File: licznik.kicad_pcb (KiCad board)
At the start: 2 copper layers, 71.1 x 44.8 mm, 24 parts, among them J1 Display, J2 Micro_SD_Card_Det, J3 Serial CS1, J4 Serial CS2, SW1 Wheel, SW2 Crank, SW3 Backlight, SW4 Right, SW5 Select, SW6 Left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

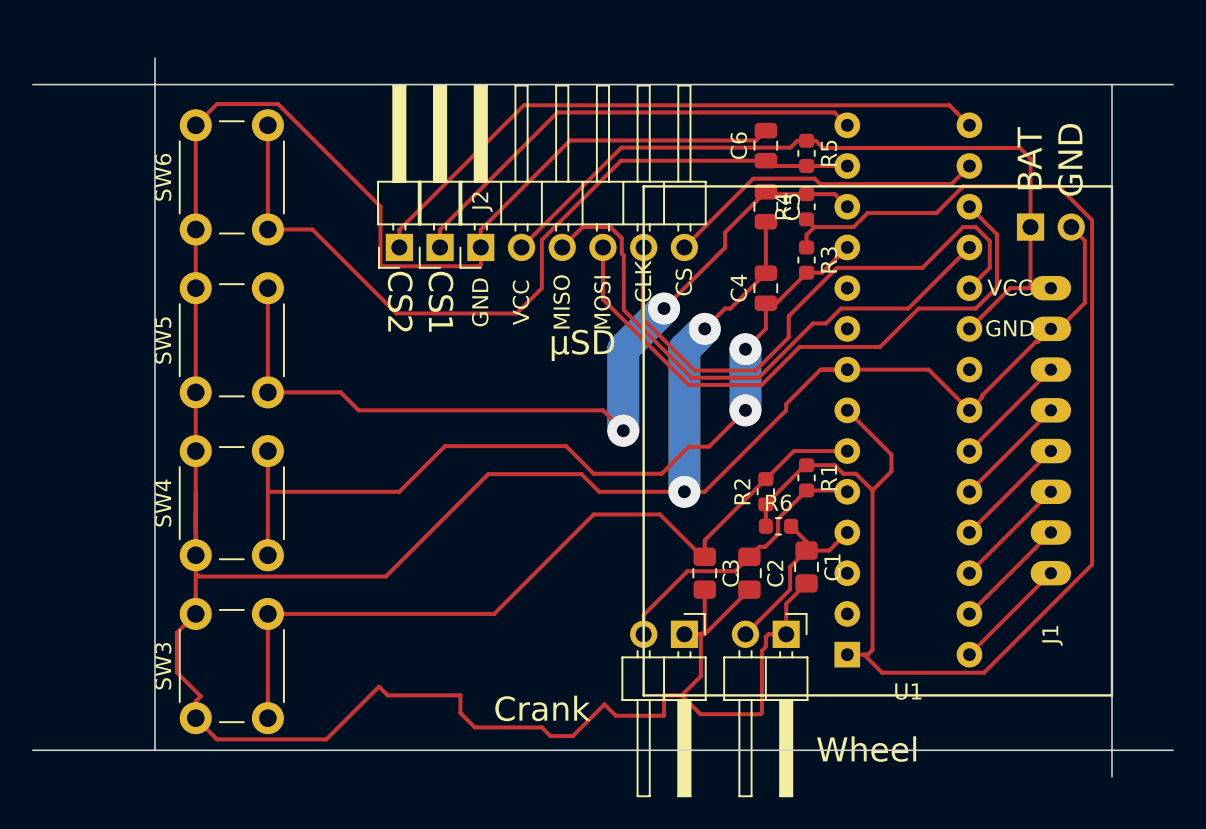
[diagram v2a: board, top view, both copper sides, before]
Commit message: Added elements for accelerometers, updated Nokia screen, shrunk the board
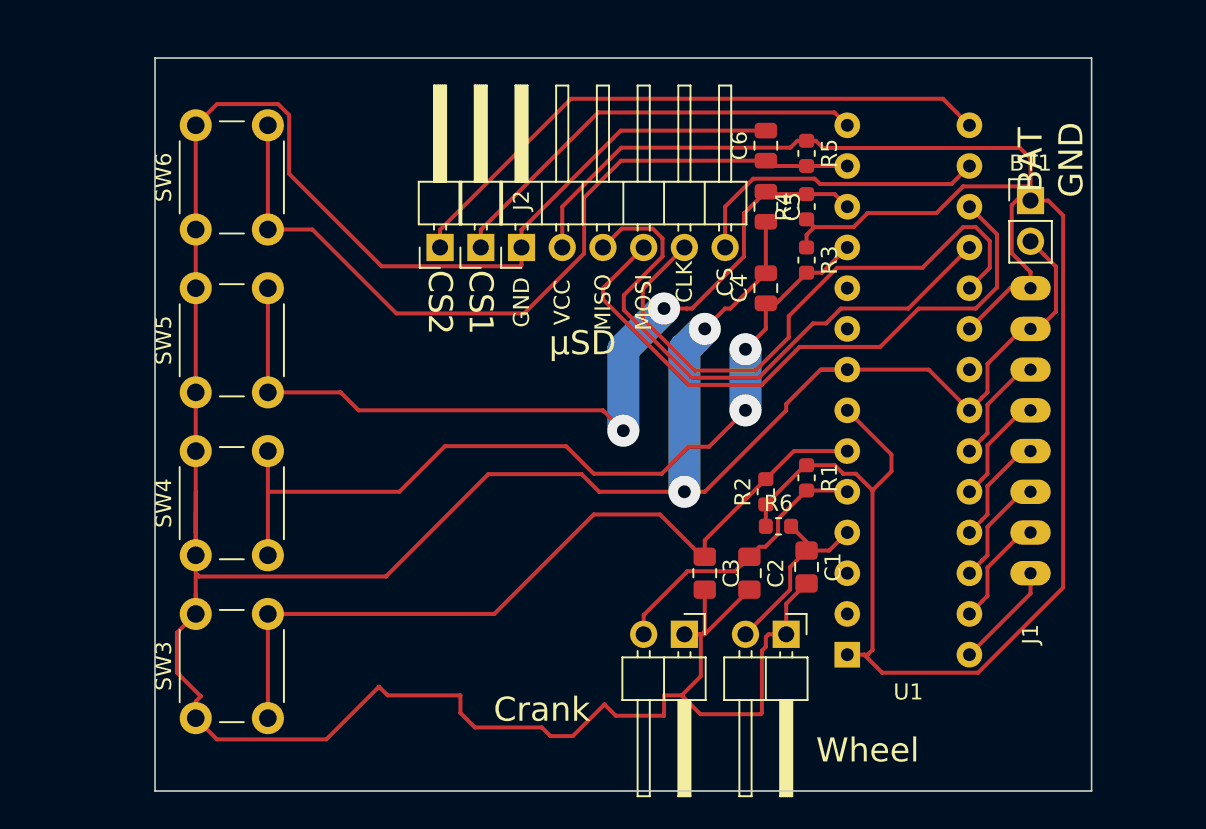
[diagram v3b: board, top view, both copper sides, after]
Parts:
- BT1: moved to F.Cu
- moved J1 5.39 mm to (87.6, 178.2)
- moved J3 2.54 mm to (53.3, 166.8)
- moved J2 2.54 mm to (55.9, 166.8)
- moved J4 2.54 mm to (50.8, 166.8)
- moved BT1 1.66 mm to (87.6, 163.8), turned to 0 degrees
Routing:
- net +BATT: track 139.3 -> 134.1 mm
- net Net-(J3-Pad1): track 29.9 -> 27.3 mm
- net Net-(J4-Pad1): track 40.4 -> 38.2 mm
- net GND: track 249.1 -> 248.0 mm
- net Net-(J2-Pad2): track 20.2 -> 19.1 mm
- net Net-(J2-Pad5): track 35.8 -> 36.8 mm
- net Net-(J2-Pad3): track 38.3 -> 39.3 mm
- net Net-(C5-Pad1): track 53.7 -> 54.7 mm
- net Net-(J2-Pad7): track 35.7 -> 36.6 mm
- net Net-(J1-Pad8): track 7.18 -> 6.66 mm
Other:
- board size 71.1 x 44.8 mm -> 58.4 x 45.7 mm

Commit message: Moved buttons closer to the middle
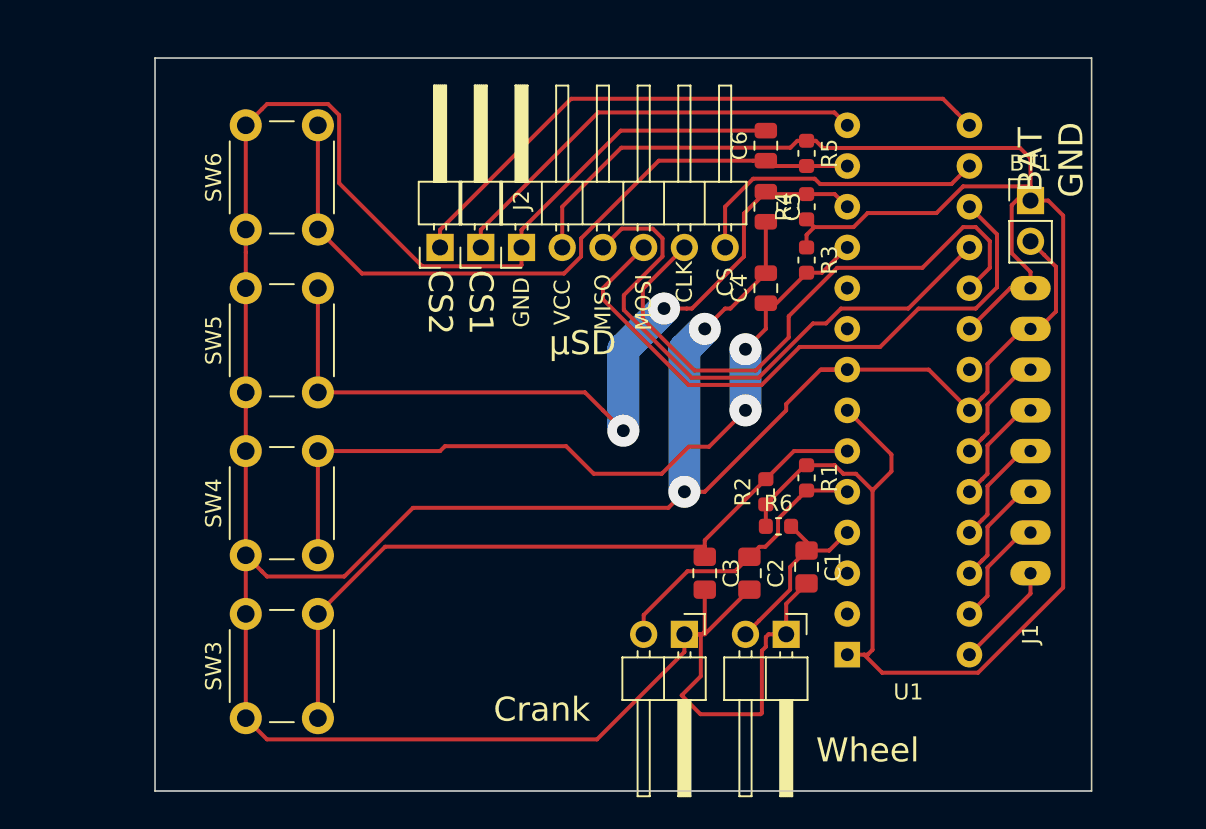
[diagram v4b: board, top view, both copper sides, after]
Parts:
- moved SW3 3.12 mm to (38.7, 196.1)
- moved SW4 3.12 mm to (38.7, 186.0)
- moved SW5 3.12 mm to (38.7, 175.8)
- moved SW6 3.12 mm to (38.7, 165.6)
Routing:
- net GND: track 248.0 -> 228.7 mm
- net Net-(C6-Pad1): track 50.9 -> 44.4 mm
- net Net-(C3-Pad1): track 50.2 -> 45.1 mm
- net Net-(C4-Pad1): track 53.3 -> 49.2 mm
- net Net-(C5-Pad1): track 54.7 -> 51.6 mm

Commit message: Spaced around components for easy soldering
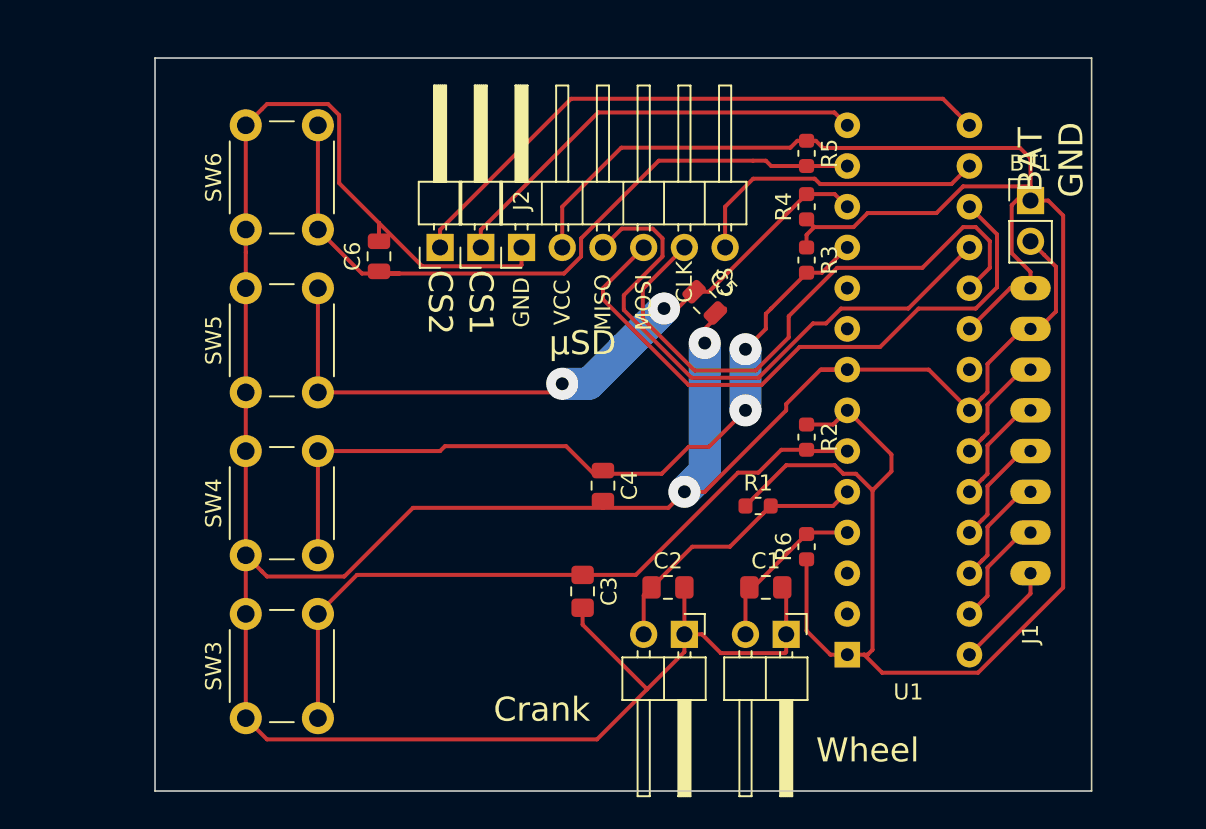
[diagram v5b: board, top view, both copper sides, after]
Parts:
- moved C6 25.1 mm to (47.0, 167.3)
- moved C4 16.0 mm to (61.0, 181.6), turned to 270 degrees
- moved C3 7.70 mm to (59.7, 188.2)
- moved C5 7.08 mm to (67.3, 170.2), turned to 315 degrees
- moved C2 5.16 mm to (65.0, 188.0), turned to 0 degrees
- moved R2 4.25 mm to (73.7, 178.6), turned to 270 degrees
- moved R1 3.49 mm to (70.6, 182.9), turned to 0 degrees
- moved C1 2.84 mm to (71.1, 188.0), turned to 0 degrees
- moved R6 2.16 mm to (73.7, 185.4), turned to 90 degrees
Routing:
- net GND: track 228.7 -> 195.6 mm
- net +BATT: track 134.1 -> 144.5 mm
- net Net-(C5-Pad1): track 51.6 -> 45.0 mm
- net Net-(C3-Pad1): track 45.1 -> 43.8 mm
- net Net-(C6-Pad1): track 44.4 -> 45.7 mm
- net Net-(C1-Pad1): track 11.7 -> 10.6 mm

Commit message: Added screen mounting holes
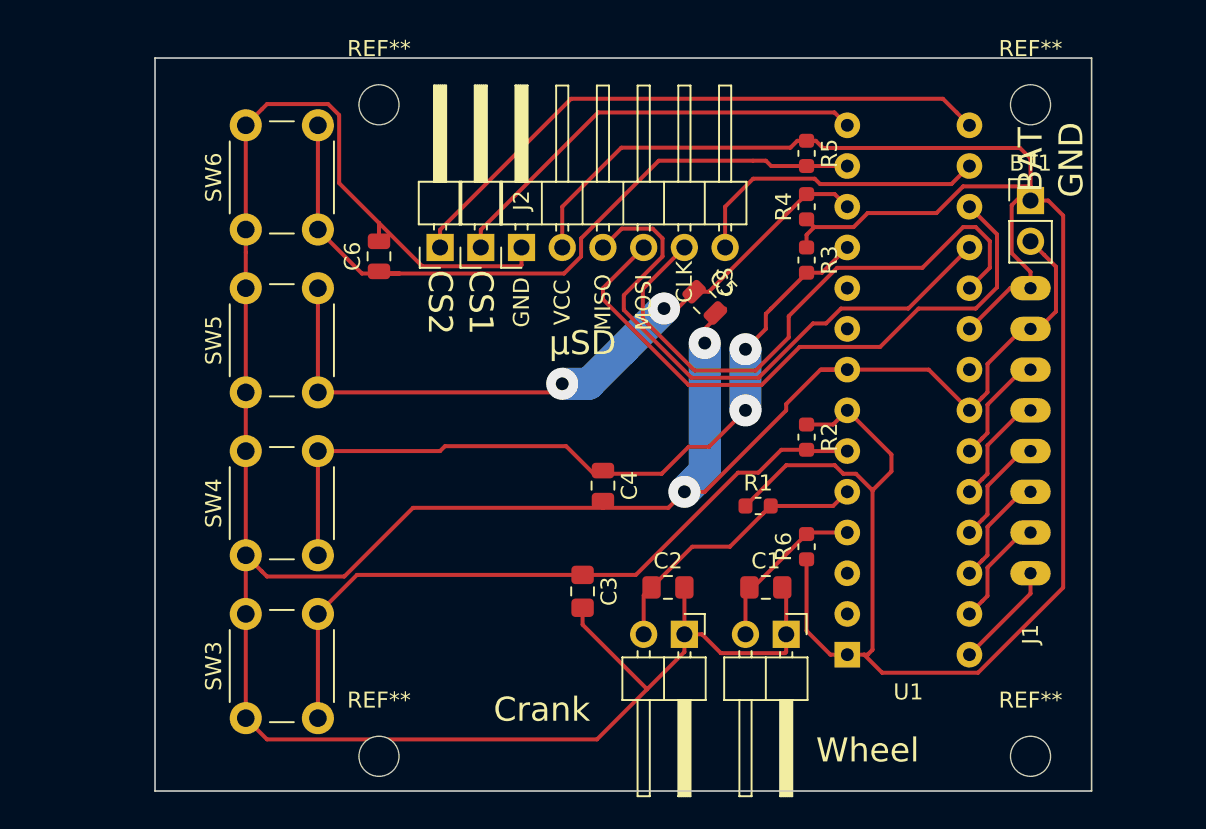
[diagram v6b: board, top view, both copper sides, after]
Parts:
- added REF**: MountingHole_2.5mm, MountingHole:MountingHole_2.5mm, F.Cu at (47.0, 157.9)
- added REF**: MountingHole_2.5mm, MountingHole:MountingHole_2.5mm, F.Cu at (87.6, 157.9)
- added REF**: MountingHole_2.5mm, MountingHole:MountingHole_2.5mm, F.Cu at (87.6, 198.5)
- added REF**: MountingHole_2.5mm, MountingHole:MountingHole_2.5mm, F.Cu at (47.0, 198.5)
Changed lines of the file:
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@@
     (tracks 264)
     (zones 0)
-    (modules 24)
+    (modules 28)
     (nets 26)
   )
@@
     (solder_mask_min_width 0.25)
     (aux_axis_origin 128.778 126.746)
-    (visible_elements FFFFFF7F)
+    (visible_elements FFFFFFFF)
     (pcbplotparams
       (layerselection 0x00030_80000001)
@@
     (uvia_drill 0.1)
   )
+  (module MountingHole:MountingHole_2.5mm (layer F.Cu)
+    (at 46.99 157.855)
+    (descr "Mounting Hole 2.5mm, no annular")
+    (tags "mounting hole 2.5mm no annular")
+    (attr virtual)
+    (fp_text reference REF** (at 0 -3.5) (layer F.SilkS)
+      (effects (font (size 1 1) (thickness 0.15)))
+    )
+    (fp_text value MountingHole_2.5mm (at 0 3.5) (layer F.Fab)
+      (effects (font (size 1 1) (thickness 0.15)))
+    )
+    (fp_text user %R (at 0.3 0) (layer F.Fab)
+      (effects (font (size 1 1) (thickness 0.15)))
+    )
+    (fp_circle (center 0 0) (end 2.5 0) (layer Cmts.User) (width 0.15))
+    (fp_circle (center 0 0) (end 2.75 0) (layer F.CrtYd) (width 0.05))
+    (pad 1 np_thru_hole circle (at 0 0) (size 2.5 2.5) (drill 2.5) (layers *.Cu *.Mask))
+  )
+  (module MountingHole:MountingHole_2.5mm (layer F.Cu)
+    (at 87.63 157.855)
+    (descr "Mounting Hole 2.5mm, no annular")
+    (tags "mounting hole 2.5mm no annular")
+    (attr virtual)
+    (fp_text reference REF** (at 0 -3.5) (layer F.SilkS)
+      (effects (font (size 1 1) (thickness 0.15)))
+    )
+    (fp_text value MountingHole_2.5mm (at 0 3.5) (layer F.Fab)
+      (effects (font (size 1 1) (thickness 0.15)))
+    )
+    (fp_text user %R (at 0.3 0) (layer F.Fab)
+      (effects (font (size 1 1) (thickness 0.15)))
+    )
+    (fp_circle (center 0 0) (end 2.5 0) (layer Cmts.User) (width 0.15))
+    (fp_circle (center 0 0) (end 2.75 0) (layer F.CrtYd) (width 0.05))
+    (pad 1 np_thru_hole circle (at 0 0) (size 2.5 2.5) (drill 2.5) (layers *.Cu *.Mask))
+  )
+  (module MountingHole:MountingHole_2.5mm (layer F.Cu)
+    (at 87.63 198.495)
+    (descr "Mounting Hole 2.5mm, no annular")
+    (tags "mounting hole 2.5mm no annular")
+    (attr virtual)
+    (fp_text reference REF** (at 0 -3.5) (layer F.SilkS)
+      (effects (font (size 1 1) (thickness 0.15)))
+    )
+    (fp_text value MountingHole_2.5mm (at 0 3.5) (layer F.Fab)
+      (effects (font (size 1 1) (thickness 0.15)))
+    )
+    (fp_text user %R (at 0.3 0) (layer F.Fab)
+      (effects (font (size 1 1) (thickness 0.15)))
+    )
+    (fp_circle (center 0 0) (end 2.5 0) (layer Cmts.User) (width 0.15))
+    (fp_circle (center 0 0) (end 2.75 0) (layer F.CrtYd) (width 0.05))
+    (pad 1 np_thru_hole circle (at 0 0) (size 2.5 2.5) (drill 2.5) (layers *.Cu *.Mask))
+  )
+  (module MountingHole:MountingHole_2.5mm (layer F.Cu)
+    (at 46.99 198.495)
+    (descr "Mounting Hole 2.5mm, no annular")
+    (tags "mounting hole 2.5mm no annular")
+    (attr virtual)
+    (fp_text reference REF** (at 0 -3.5) (layer F.SilkS)
+      (effects (font (size 1 1) (thickness 0.15)))
+    )
+    (fp_text value MountingHole_2.5mm (at 0 3.5) (layer F.Fab)
+      (effects (font (size 1 1) (thickness 0.15)))
+    )
+    (fp_circle (center 0 0) (end 2.75 0) (layer F.CrtYd) (width 0.05))
+    (fp_circle (center 0 0) (end 2.5 0) (layer Cmts.User) (width 0.15))
+    (fp_text user %R (at 0.3 0) (layer F.Fab)
+      (effects (font (size 1 1) (thickness 0.15)))
+    )
+    (pad 1 np_thru_hole circle (at 0 0) (size 2.5 2.5) (drill 2.5) (layers *.Cu *.Mask))
+  )
   (module "Licznik:Nokia screen" (layer F.Cu)

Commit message: Added logo
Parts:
- added logo: G***, Licznik:logo_half, F.Cu at (53.3, 191.8)

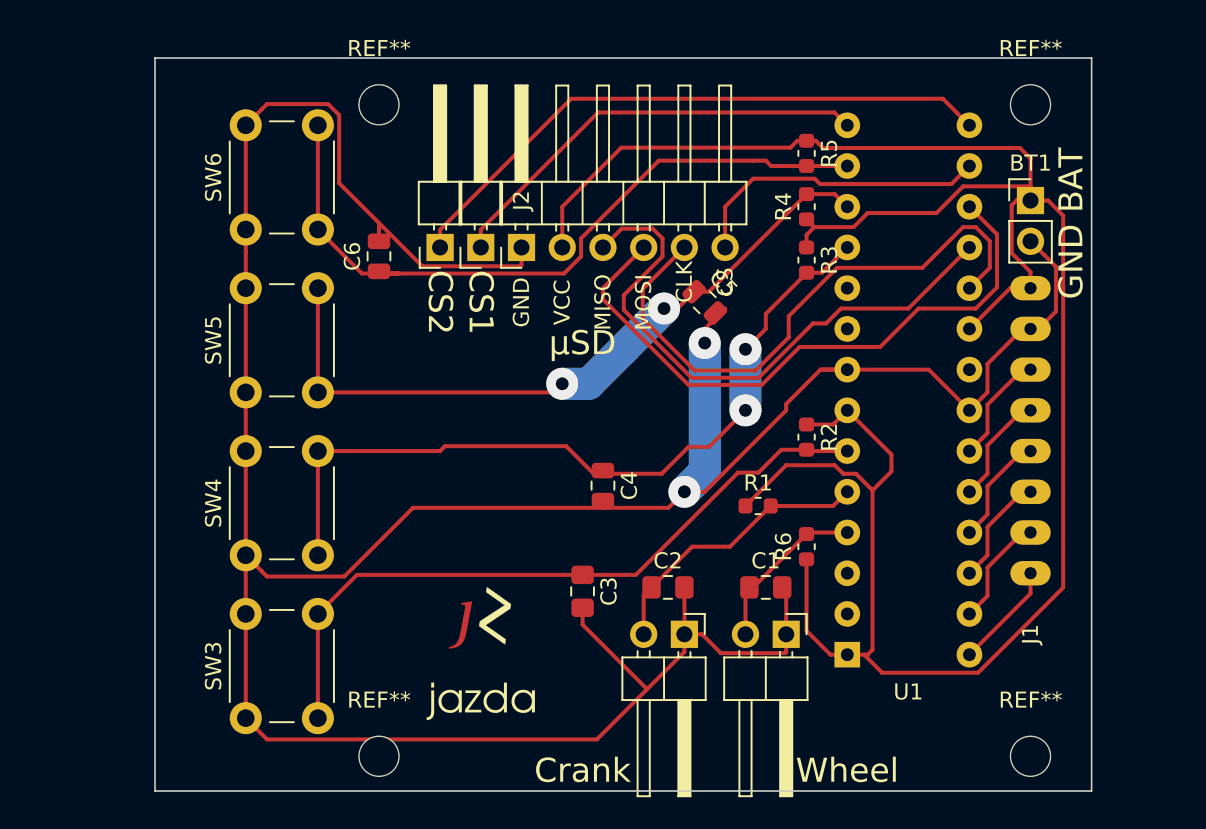
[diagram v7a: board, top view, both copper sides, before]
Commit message: Added silkscreen logos, placed silkscreen properly
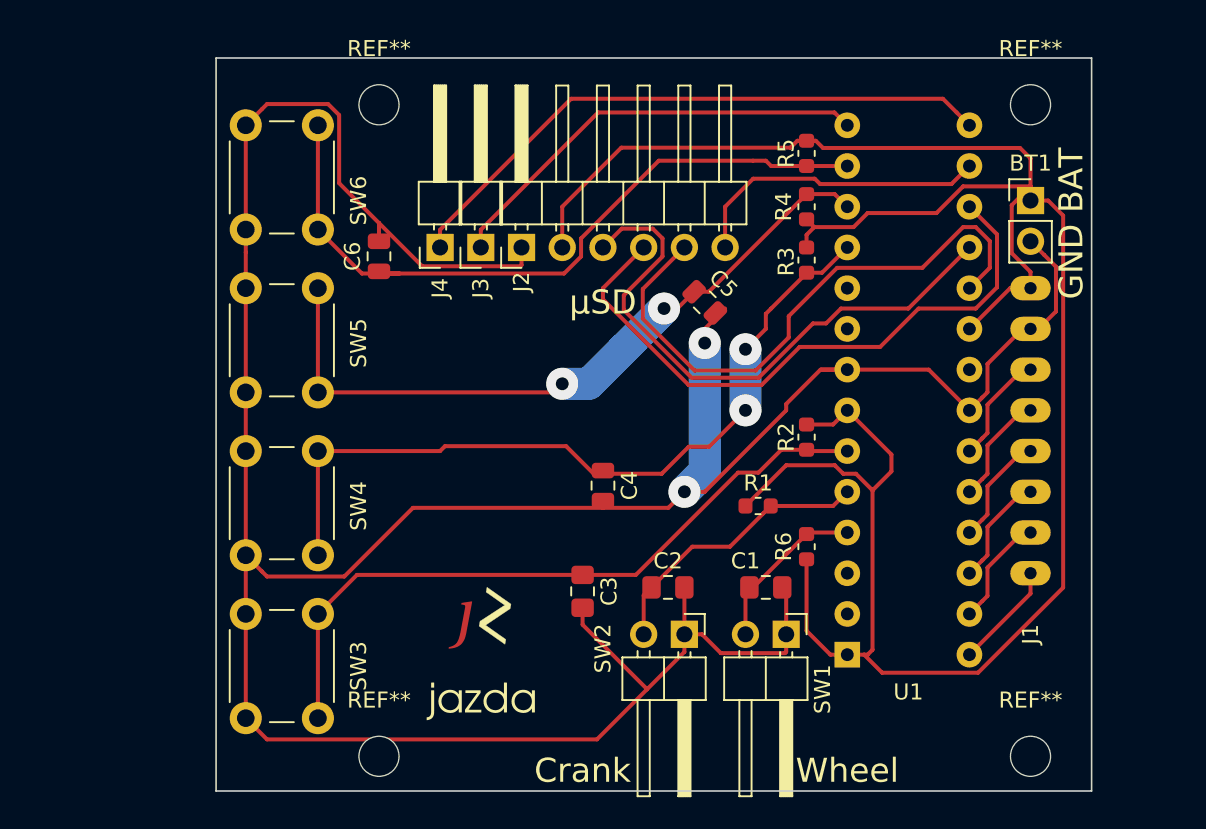
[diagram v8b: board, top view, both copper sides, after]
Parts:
- added REF**: OSHW-Logo2_7.3x6mm_SilkScreen, Symbol:OSHW-Logo2_7.3x6mm_SilkScreen, B.Cu at (53.3, 175.3)
- added REF**: KiCad-Logo2_6mm_SilkScreen, Symbol:KiCad-Logo2_6mm_SilkScreen, B.Cu at (68.6, 186.7)
- added logo: G***, Licznik:logo_ss, B.Cu at (54.6, 189.2)
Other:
- board size 58.4 x 45.7 mm -> 54.6 x 45.7 mm
